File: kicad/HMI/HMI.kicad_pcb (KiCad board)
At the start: 2 copper layers, 47 x 107.2 mm, 59 parts, among them J2 SWD, J3 FH12-22S-0.5SH, J4 RIBBON, SW1 SW_Push, SW10 SW_Push, SW11 SW_Push, SW12 SW_Push, SW13 SW_Push, SW14 SW_Push, SW15 SW_Push, SW16 SW_Push, SW17 SW_Push, SW18 SW_Push, SW19 SW_Push, SW2 SW_Push, SW20 SW_Push, SW3 SW_Push, SW4 SW_Push, SW5 SW_Push, SW6 SW_Push, SW7 SW_Push, SW8 SW_Push, SW9 SW_Push, U1 STM32L011K4Tx, U2 DEM 128128A TMH-PW-N, X1 ASV-4.000MHZ-EJ-T

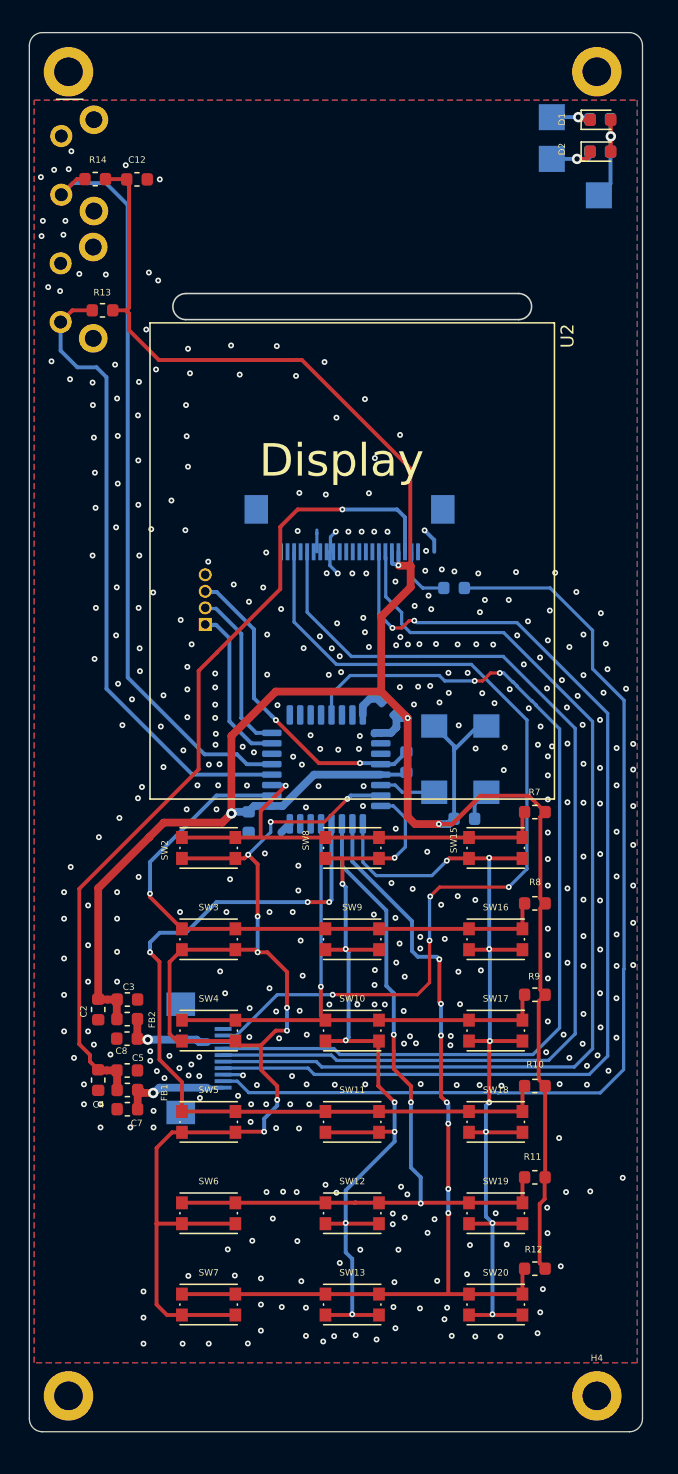
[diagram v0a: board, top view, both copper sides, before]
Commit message: Add thermals on ground plane, extend ground plane to PCB edges
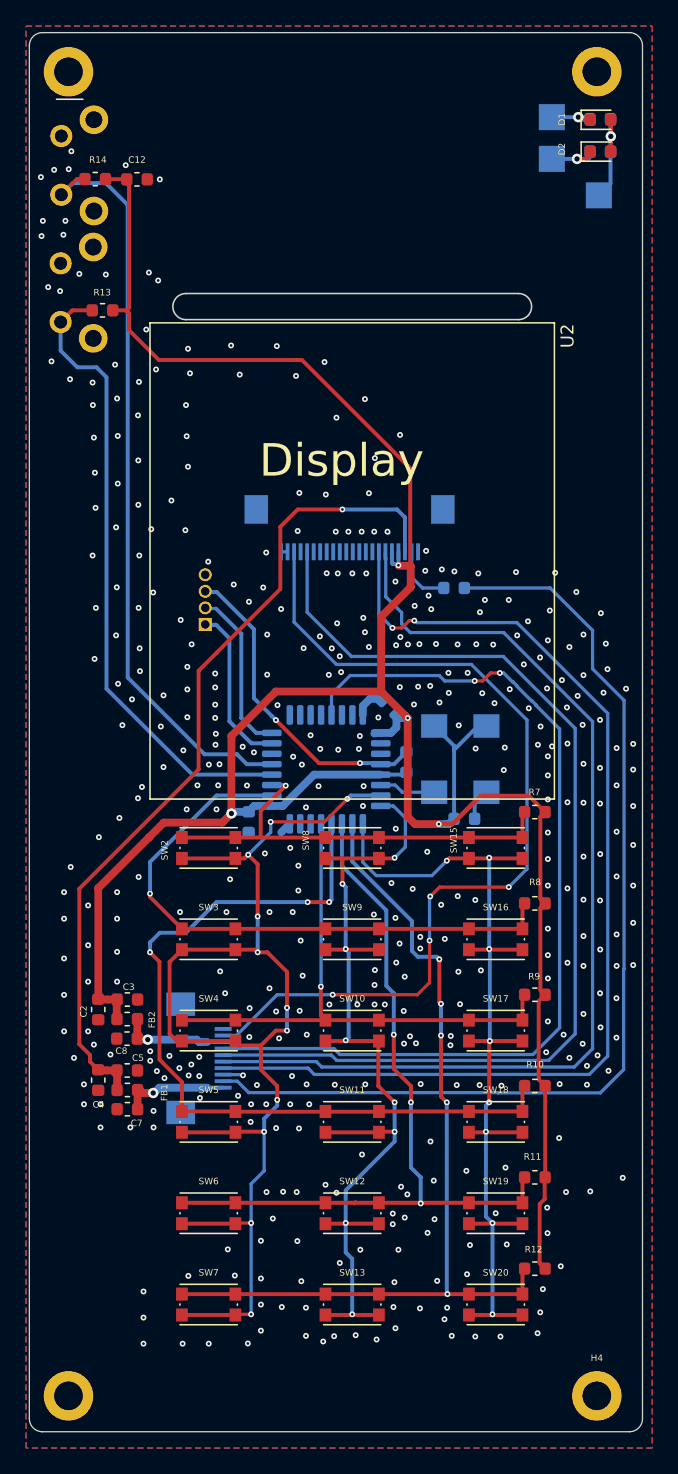
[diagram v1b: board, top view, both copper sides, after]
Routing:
- net GND: track 14.7 -> 7.92 mm, vias 415 -> 421
- net C1: track 96.2 -> 94.4 mm, vias 9 -> 11
- net R1: track 68.2 -> 68.0 mm, vias 7 -> 5

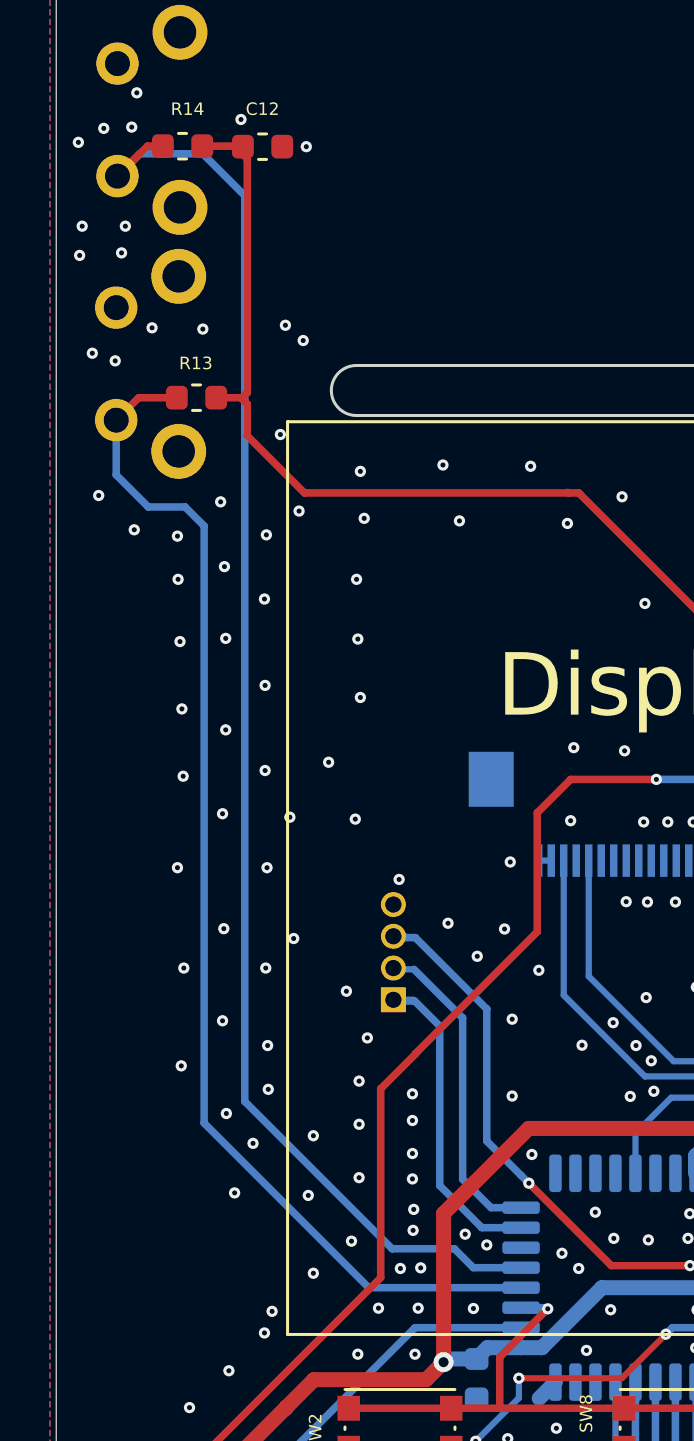
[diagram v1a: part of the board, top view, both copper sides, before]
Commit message: Relocating J2 from underneath display
This is a temporary fix. With issue #7, this part will change.
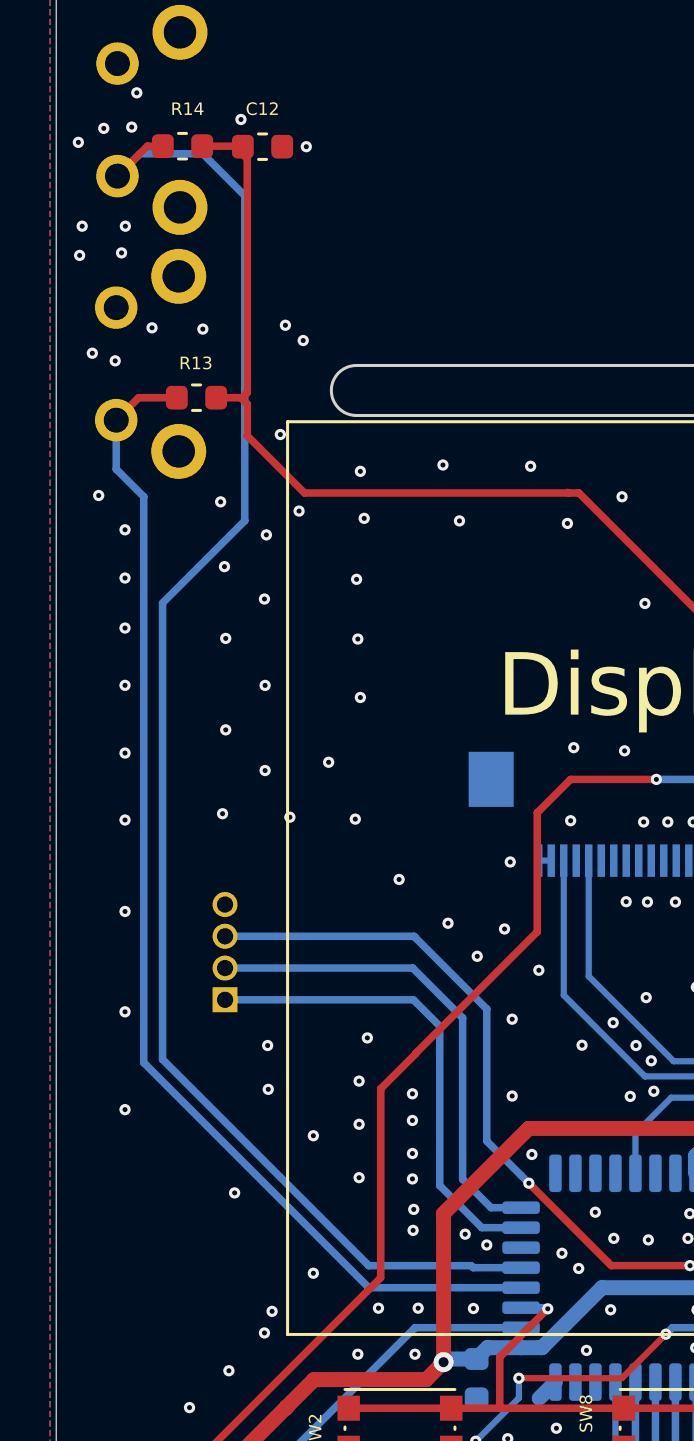
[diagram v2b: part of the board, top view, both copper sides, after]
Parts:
- moved J2 6.73 mm to (125.0, 79.9)
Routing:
- net SWCLK: track 12.9 -> 19.6 mm
- net NRST: track 24.9 -> 31.1 mm
- net SWDIO: track 13.4 -> 19.3 mm
- net F2: track 58.5 -> 62.2 mm
- net F1: track 49.4 -> 48.6 mm
- net GND: vias 421 -> 409
